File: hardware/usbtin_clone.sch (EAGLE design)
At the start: 29 parts, among them IC1 18F14K50, IC3 MCP2551

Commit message: add vallues to schematic
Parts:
- C1, C2: value (none) -> 22p
- C3, C4, C5, C6, C7, C8: value (none) -> 100n
- C9: value (none) -> 4,7u
- R1, R2, R5, R6, R9: value (none) -> 390
- R3: value (none) -> 120
- R4, R7, R8: value (none) -> 1k

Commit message: 5V clearance
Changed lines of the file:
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@@
 <part name="C6" library="resistor" deviceset="C-EU" device="025-025X050" value="100n"/>
 <part name="C7" library="resistor" deviceset="C-EU" device="025-025X050" value="100n"/>
-<part name="P+5" library="supply1" deviceset="VCC/2" device=""/>
+<part name="P+5" library="supply1" deviceset="VCC/2" device="" value="5V"/>
 <part name="GND6" library="supply1" deviceset="GNDA" device=""/>
-<part name="P+6" library="supply1" deviceset="VCC/2" device=""/>
+<part name="P+6" library="supply1" deviceset="VCC/2" device="" value="5V"/>
 <part name="GND7" library="supply1" deviceset="GNDA" device=""/>
 <part name="P+7" library="supply1" deviceset="VCC" device=""/>
@@
 <part name="P+9" library="supply1" deviceset="VCC/2" device="" value="5V"/>
 <part name="P+10" library="supply1" deviceset="VCC" device=""/>
-<part name="P+11" library="supply1" deviceset="VCC/2" device=""/>
+<part name="P+11" library="supply1" deviceset="VCC/2" device="" value="5V"/>
 <part name="GND10" library="supply1" deviceset="GNDA" device=""/>
 <part name="GND11" library="supply1" deviceset="GNDA" device=""/>

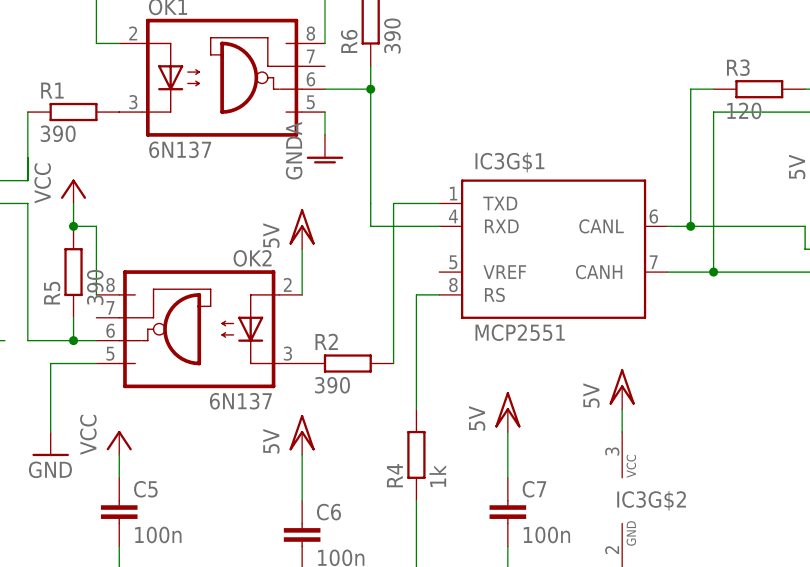
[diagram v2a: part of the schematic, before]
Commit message: grr - CAN TX/RX fault
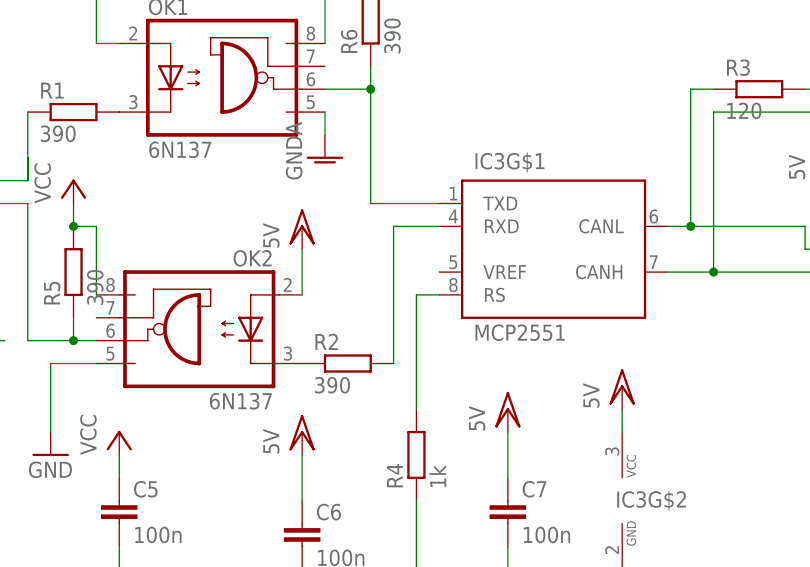
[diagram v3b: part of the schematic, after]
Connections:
- net N$6: now also IC3G$1.TXD; no longer IC3G$1.RXD
- net N$8: now also IC3G$1.RXD; no longer IC3G$1.TXD
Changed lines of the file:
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@@
 <wire x1="149.86" y1="60.96" x2="154.94" y2="60.96" width="0.1524" layer="91"/>
 <wire x1="154.94" y1="60.96" x2="154.94" y2="48.26" width="0.1524" layer="91"/>
-<pinref part="IC3" gate="G$1" pin="RXD"/>
-<wire x1="154.94" y1="48.26" x2="154.94" y2="45.72" width="0.1524" layer="91"/>
-<wire x1="154.94" y1="45.72" x2="162.56" y2="45.72" width="0.1524" layer="91"/>
 <pinref part="R6" gate="G$1" pin="1"/>
 <wire x1="154.94" y1="60.96" x2="154.94" y2="63.5" width="0.1524" layer="91"/>
 <junction x="154.94" y="60.96"/>
-</segment>
-</net>
-<net name="N$8" class="0">
-<segment>
-<pinref part="R2" gate="G$1" pin="2"/>
-<wire x1="157.48" y1="30.48" x2="157.48" y2="45.72" width="0.1524" layer="91"/>
 <pinref part="IC3" gate="G$1" pin="TXD"/>
-<wire x1="157.48" y1="45.72" x2="157.48" y2="48.26" width="0.1524" layer="91"/>
-<wire x1="157.48" y1="48.26" x2="162.56" y2="48.26" width="0.1524" layer="91"/>
+<wire x1="154.94" y1="48.26" x2="162.56" y2="48.26" width="0.1524" layer="91"/>
 </segment>
 </net>
@@
 </segment>
 </net>
+<net name="N$8" class="0">
+<segment>
+<pinref part="IC3" gate="G$1" pin="RXD"/>
+<pinref part="R2" gate="G$1" pin="2"/>
+<wire x1="162.56" y1="45.72" x2="157.48" y2="45.72" width="0.1524" layer="91"/>
+<wire x1="157.48" y1="45.72" x2="157.48" y2="30.48" width="0.1524" layer="91"/>
+</segment>
+</net>
